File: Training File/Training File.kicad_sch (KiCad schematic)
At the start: 0 parts

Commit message: CAN reciever
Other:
- added sheet CAN (Can.Kicad_sch)
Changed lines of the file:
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@@
+		)
+	)
+	(sheet
+		(at 27.94 59.69)
+		(size 78.74 45.72)
+		(exclude_from_sim no)
+		(in_bom yes)
+		(on_board yes)
+		(dnp no)
+		(fields_autoplaced yes)
+		(stroke
+			(width 0.1524)
+			(type solid)
+		)
+		(fill
+			(color 0 0 0 0.0000)
+		)
+		(property "Sheetname" "CAN"
+			(at 27.94 58.9784 0)
+			(effects
+				(font
+					(size 1.27 1.27)
+				)
+				(justify left bottom)
+			)
+		)
+		(property "Sheetfile" "Can.Kicad_sch"
+			(at 27.94 105.9946 0)
+			(effects
+				(font
+					(size 1.27 1.27)
+				)
+				(justify left top)
+			)
+		)
+		(instances
+			(project "Training File"
+				(path "/d3b46590-8d43-4cdb-9712-6960f55d7470"
+					(page "4")
+				)
+			)
 		)
 	)

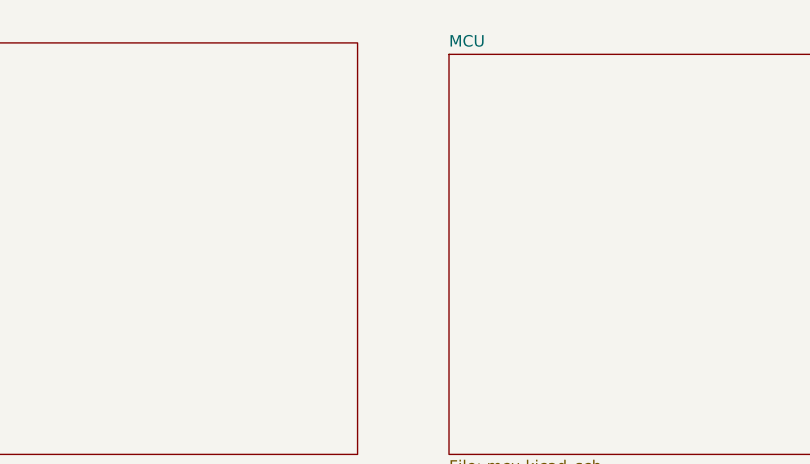
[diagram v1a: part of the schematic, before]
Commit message: Finish schematic
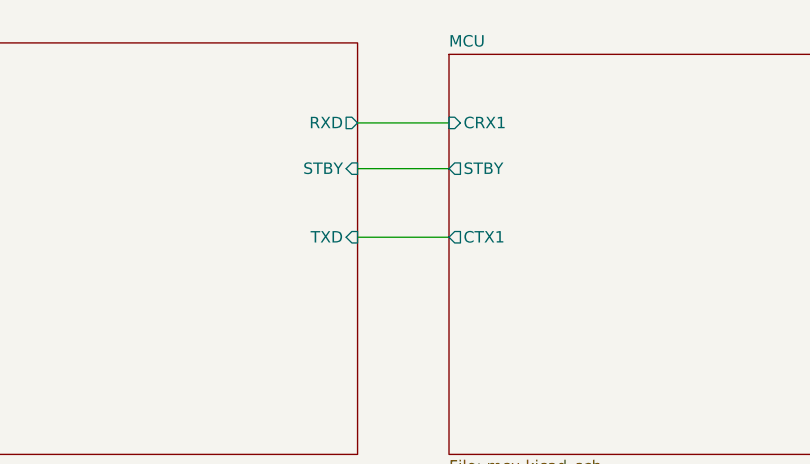
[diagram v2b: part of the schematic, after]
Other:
- sheet CAN ports: added RXD, STBY, TXD; removed none
- sheet MCU ports: added CRX1, CTX1, STBY; removed none
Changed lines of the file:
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@@
 	(generator_version "9.0")
 	(paper "A4")
+	(wire
+		(pts
+			(xy 106.68 73.66) (xy 116.84 73.66)
+		)
+		(stroke
+			(width 0)
+			(type default)
+		)
+	)
+	(wire
+		(pts
+			(xy 106.68 81.28) (xy 116.84 81.28)
+		)
+		(stroke
+			(width 0)
+			(type default)
+		)
+	)
+	(wire
+		(pts
+			(xy 106.68 68.58) (xy 116.84 68.58)
+		)
+		(stroke
+			(width 0)
+			(type default)
+		)
+	)
 	(sheet
 		(at 116.84 60.96)
@@
 				)
 				(justify left top)
+			)
+		)
+		(pin "CRX1" input
+			(at 116.84 68.58 180)
+			(effects
+				(font
+					(size 1.27 1.27)
+				)
+				(justify left)
+			)
+		)
+		(pin "CTX1" output
+			(at 116.84 81.28 180)
+			(effects
+				(font
+					(size 1.27 1.27)
+				)
+				(justify left)
+			)
+		)
+		(pin "STBY" output
+			(at 116.84 73.66 180)
+			(effects
+				(font
+					(size 1.27 1.27)
+				)
+				(justify left)
 			)
 		)
@@
 			)
 		)
+		(pin "RXD" output
+			(at 106.68 68.58 0)
+			(effects
+				(font
+					(size 1.27 1.27)
+				)
+				(justify right)
+			)
+		)
+		(pin "STBY" input
+			(at 106.68 73.66 0)
+			(effects
+				(font
+					(size 1.27 1.27)
+				)
+				(justify right)
+			)
+		)
+		(pin "TXD" input
+			(at 106.68 81.28 0)
+			(effects
+				(font
+					(size 1.27 1.27)
+				)
+				(justify right)
+			)
+		)
